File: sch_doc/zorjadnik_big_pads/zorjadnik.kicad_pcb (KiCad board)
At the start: 2 copper layers, 65 parts, among them J1 Conn_01x01, J10 Screw_Terminal_01x02, J11 Screw_Terminal_01x02, J12 Conn_01x02, J2 Conn_01x01, J3 Conn_01x01, J4 Conn_01x01, J5 Conn_01x08, J6 Conn_01x03, J7 Conn_01x02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

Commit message: навел красивостей в схеме
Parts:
- C11, C12: value CP -> 10µF
- J1: value Conn_01x01 -> OUT1
- J10: value Screw_Terminal_01x02 -> output GND
- J11: value Screw_Terminal_01x02 -> power supply GND
- J12: value Conn_01x02 -> spare port
- J2: value Conn_01x01 -> OUT2
- J3: value Conn_01x01 -> Vsb
- J4: value Conn_01x01 -> GND
- J5: value Conn_01x08 -> display module
- J6: value Conn_01x03 -> firmware
- J7: value Conn_01x02 -> cooling fan
- J8: value Conn_01x08 -> driver
- J9: value Conn_01x01 -> power supply Vout
- L1: value L_Small -> 47µH; footprint Inductor_SMD:L_1206_3216Metric -> Inductor_SMD:L_1210_3225Metric
- R10, R11, R12, R13, R4, R5, R6, R7, R8, R9: value 1R -> 0.1R
- R14, R15: value R -> 100
- R20, R21, R22: value 300 -> 200
- moved CB2 9.84 mm to (32.7, 66.9)
- moved CB1 9.75 mm to (32.7, 76.7)
- moved L1 4.18 mm to (55.9, 36.0)
- moved R24 1.91 mm to (43.0, 26.8)
- moved D3 1.19 mm to (52.5, 35.6), turned to 180 degrees
- moved C11 0.47 mm to (45.5, 33.5)
- moved D6 0.44 mm to (49.6, 32.9)
- moved C4 0.32 mm to (46.3, 35.4)
- moved C1 0.29 mm to (49.3, 35.4)
- moved U1 0.23 mm to (47.5, 40.6)
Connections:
- net /con3 renamed /pot
- net /con5 renamed /SCK
- net /con6 renamed /ST_CP
- net /con7 renamed /MOSI
- R14 pad 1: Net-(CB2-Pad2) -> Net-(CB1-Pad2)
- R15 pad 1: Net-(CB1-Pad2) -> Net-(CB2-Pad2)
- R20 pad 1: /Sheet5D41F71D/D3 -> Net-(D1-Pad8)
- R20 pad 2: Net-(D1-Pad8) -> /Sheet5D41F71D/D3
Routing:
- net +3V3: track 38.2 -> 73.6 mm
- net Net-(CB2-Pad2): track 9.37 -> 22.1 mm
- net Net-(CB1-Pad2): track 22.1 -> 9.37 mm
- net Net-(C12-Pad1): track 20.7 -> 19.5 mm
- net +VDC: track 26.0 -> 26.9 mm
- net Net-(C1-Pad1): track 8.82 -> 8.21 mm
- net GND: track 352.8 -> 353.4 mm

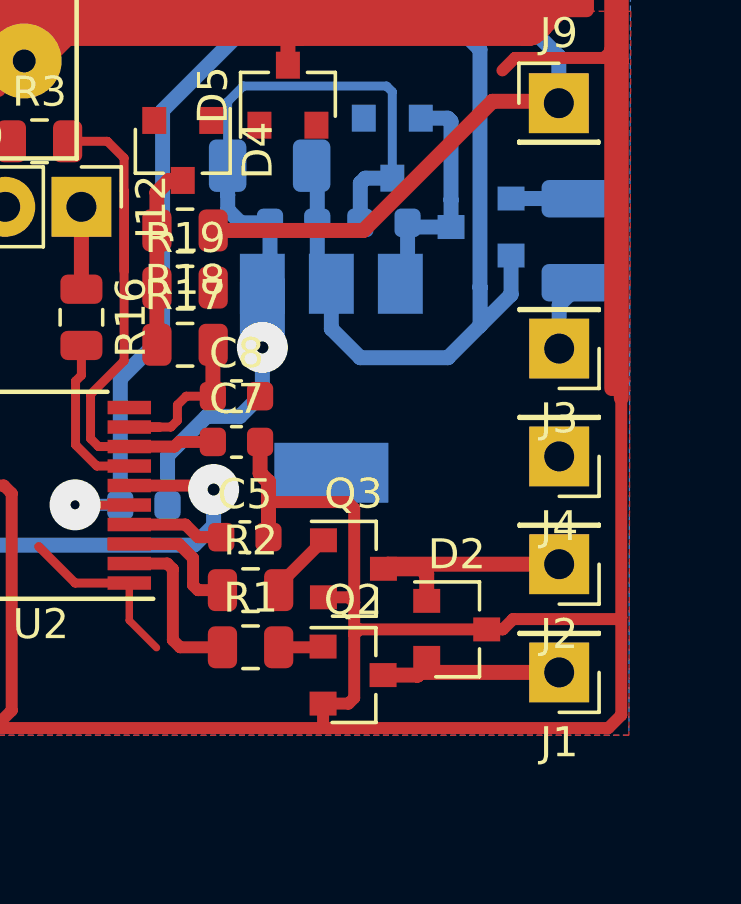
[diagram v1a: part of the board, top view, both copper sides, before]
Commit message: навел порядок в datasheets
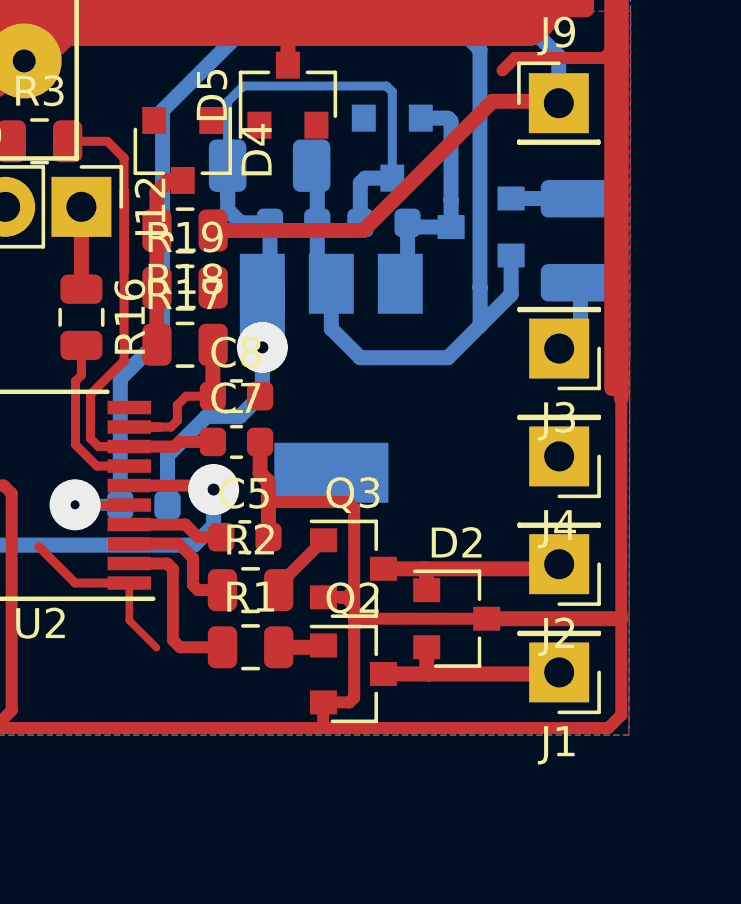
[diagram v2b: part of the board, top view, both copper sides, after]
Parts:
- moved D2 0.36 mm to (51.7, 48.6)
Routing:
- net Net-(D2-Pad1): track 8.33 -> 6.66 mm
- net GND: track 353.4 -> 354.3 mm
- net +28V: track 3.06 -> 2.49 mm

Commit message: что то подкрутил
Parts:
- C2: moved to F.Cu
- moved C2 3.92 mm to (45.2, 44.3)
- moved D6 0.83 mm to (50.4, 32.9)
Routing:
- net GND: track 354.3 -> 342.8 mm
- net /pot: track 25.9 -> 19.7 mm
- net Net-(C1-Pad1): track 8.21 -> 7.34 mm

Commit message: поаккуратней схема
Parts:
- moved R15 1.92 mm to (30.8, 87.0)
- turned R20 to 270 degrees
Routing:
- net GND: track 342.8 -> 374.0 mm
- net Net-(J8-Pad2): track 12.0 -> 14.0 mm
- net Net-(J8-Pad6): track 24.5 -> 25.5 mm
- net +3V3: track 73.4 -> 74.3 mm
- net Net-(J8-Pad5): track 24.9 -> 24.0 mm
- net Net-(CB2-Pad2): track 22.1 -> 21.3 mm
